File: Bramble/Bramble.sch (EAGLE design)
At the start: 10 parts

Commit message: Upgrades
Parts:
- added C1, C2, C3, C4, C5, C6, C7, C8: (no value), cap-master:CBP-ENP-020-050
- added F1: FUSEBLANK_5X20MM, fuse:FUSEBLANK_5X20MM
- added L1, L2, L3, L4, L5, L6, L7, L8: BL01RN1A, inductors:BL01RN1A
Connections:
- new net N$1: C1.1, L1.1, PWR1.VBUS
- new net N$2: C2.1, L2.1, PWR2.VBUS
- new net N$3: C4.1, L4.1, PWR4.VBUS
- new net N$4: C3.1, L3.1, PWR3.VBUS
- new net N$5: C5.1, L5.1, PWR5.VBUS
- new net N$6: C6.1, L6.1, PWR6.VBUS
- new net N$7: C7.1, L7.1, PWR7.VBUS
- new net N$8: C8.1, L8.1, PWR8.VBUS
- new net N$9: F1.2, PWR_IN-1.KL
- net 5V: now also L1.2, L2.2, L3.2, L4.2, L5.2, L6.2, L7.2, L8.2; no longer PWR1.VBUS, PWR2.VBUS, PWR3.VBUS, PWR4.VBUS, PWR5.VBUS, PWR6.VBUS, PWR7.VBUS, PWR8.VBUS, PWR_IN-1.KL
- net GND: now also C1.2, C2.2, C3.2, C4.2, C5.2, C6.2, C7.2, C8.2
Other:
- moved on the sheet: PWR1, PWR2, PWR3, PWR4

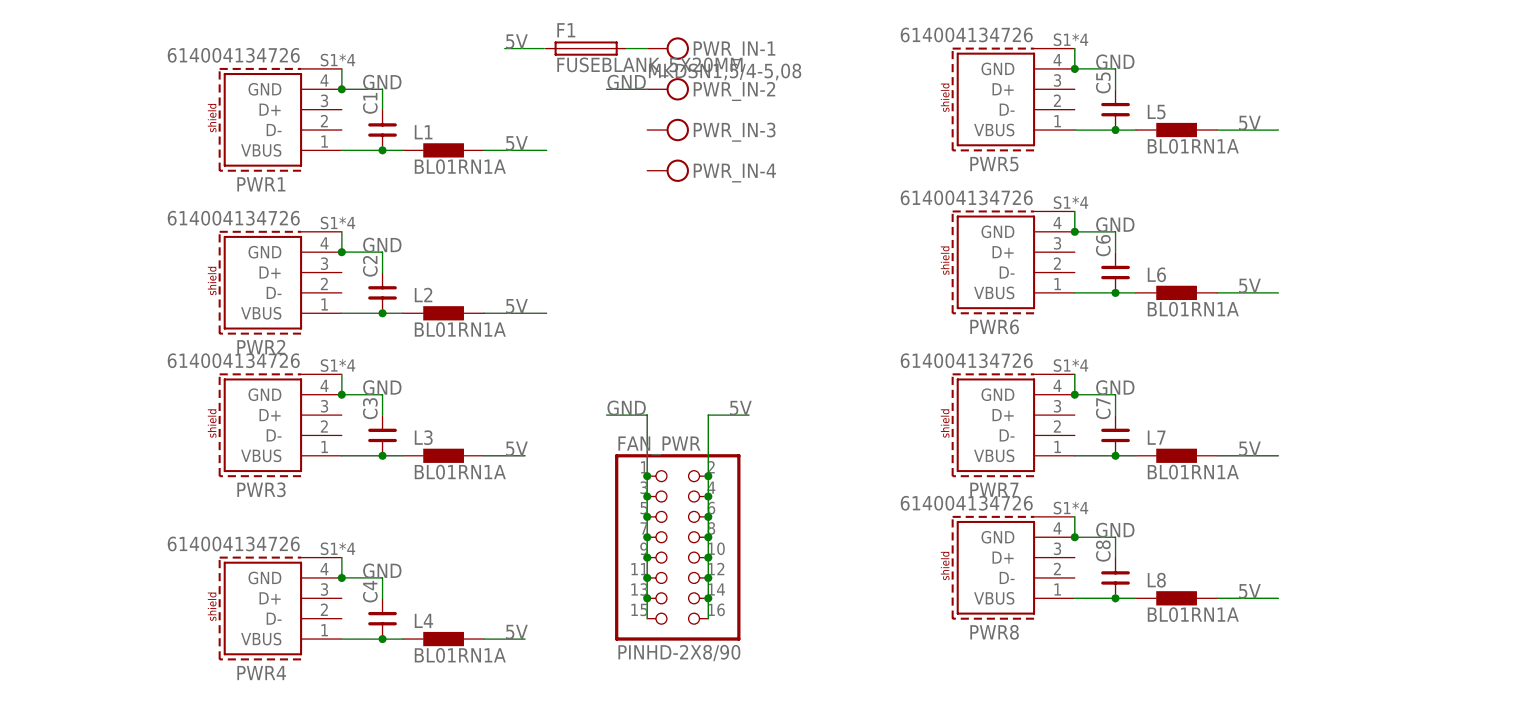
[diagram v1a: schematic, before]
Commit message: Capacitors among USB connectors
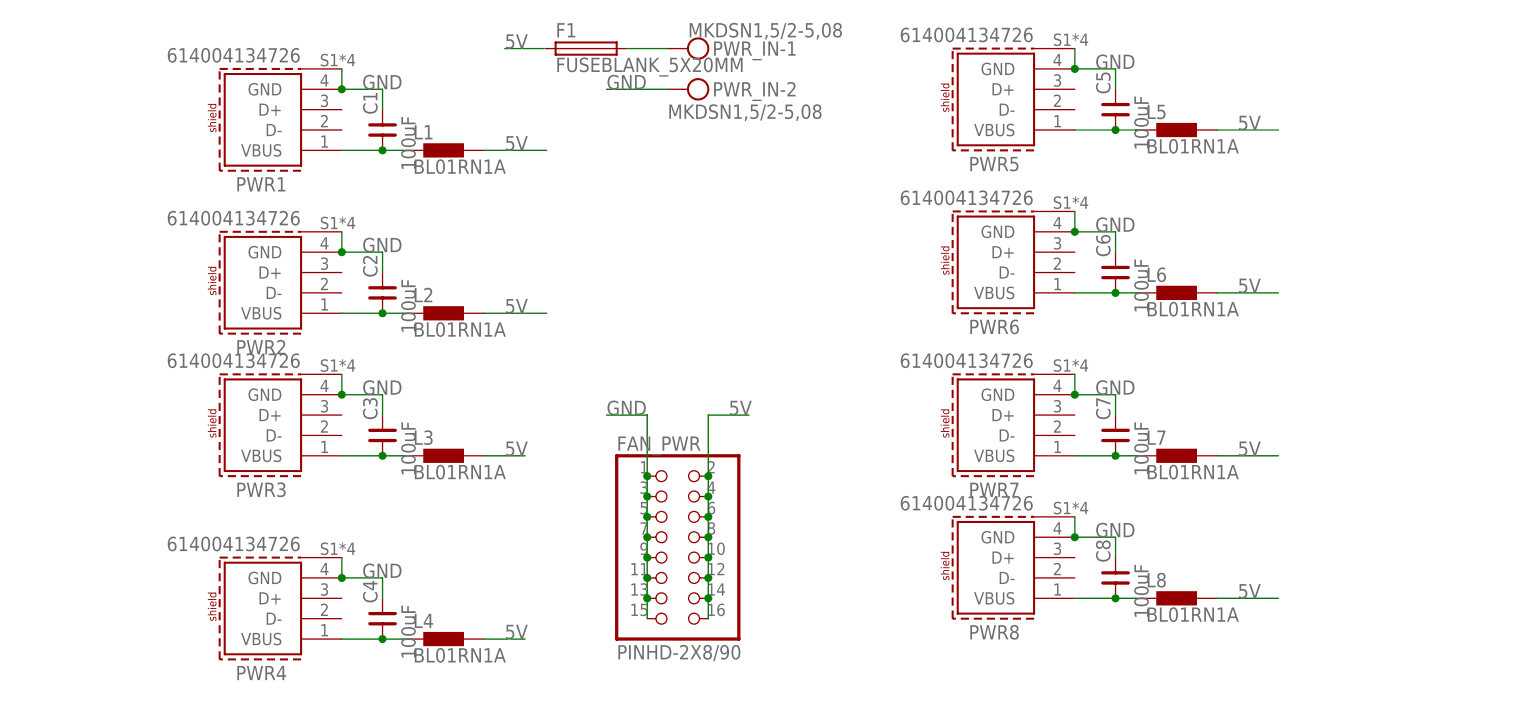
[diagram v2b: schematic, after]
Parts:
- C1, C2, C3, C4, C5, C6, C7, C8: value (none) -> 100uF
- PWR_IN: value MKDSN1,5/4-5,08 -> MKDSN1,5/2-5,08; device con-phoenix-508:MKDSN1,5/4-5,08 -> con-phoenix-508:MKDSN1,5/2-5,08
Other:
- moved on the sheet: PWR_IN-1, PWR_IN-2
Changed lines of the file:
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@@
 <grid distance="0.1" unitdist="inch" unit="inch" style="lines" multiple="1" display="no" altdistance="0.01" altunitdist="inch" altunit="inch"/>
 <layers>
-<layer number="1" name="Top" color="4" fill="1" visible="yes" active="no"/>
-<layer number="16" name="Bottom" color="1" fill="1" visible="yes" active="no"/>
-<layer number="17" name="Pads" color="2" fill="1" visible="yes" active="no"/>
-<layer number="18" name="Vias" color="2" fill="1" visible="yes" active="no"/>
-<layer number="19" name="Unrouted" color="6" fill="1" visible="yes" active="no"/>
-<layer number="20" name="Dimension" color="24" fill="1" visible="yes" active="no"/>
-<layer number="21" name="tPlace" color="7" fill="1" visible="yes" active="no"/>
-<layer number="22" name="bPlace" color="7" fill="1" visible="yes" active="no"/>
-<layer number="23" name="tOrigins" color="15" fill="1" visible="yes" active="no"/>
-<layer number="24" name="bOrigins" color="15" fill="1" visible="yes" active="no"/>
-<layer number="25" name="tNames" color="7" fill="1" visible="yes" active="no"/>
-<layer number="26" name="bNames" color="7" fill="1" visible="yes" active="no"/>
-<layer number="27" name="tValues" color="7" fill="1" visible="yes" active="no"/>
-<layer number="28" name="bValues" color="7" fill="1" visible="yes" active="no"/>
+<layer number="1" name="Top" color="4" fill="1" visible="no" active="no"/>
+<layer number="16" name="Bottom" color="1" fill="1" visible="no" active="no"/>
+<layer number="17" name="Pads" color="2" fill="1" visible="no" active="no"/>
+<layer number="18" name="Vias" color="2" fill="1" visible="no" active="no"/>
+<layer number="19" name="Unrouted" color="6" fill="1" visible="no" active="no"/>
+<layer number="20" name="Dimension" color="24" fill="1" visible="no" active="no"/>
+<layer number="21" name="tPlace" color="7" fill="1" visible="no" active="no"/>
+<layer number="22" name="bPlace" color="7" fill="1" visible="no" active="no"/>
+<layer number="23" name="tOrigins" color="15" fill="1" visible="no" active="no"/>
+<layer number="24" name="bOrigins" color="15" fill="1" visible="no" active="no"/>
+<layer number="25" name="tNames" color="7" fill="1" visible="no" active="no"/>
+<layer number="26" name="bNames" color="7" fill="1" visible="no" active="no"/>
+<layer number="27" name="tValues" color="7" fill="1" visible="no" active="no"/>
+<layer number="28" name="bValues" color="7" fill="1" visible="no" active="no"/>
 <layer number="29" name="tStop" color="7" fill="3" visible="no" active="no"/>
 <layer number="30" name="bStop" color="7" fill="6" visible="no" active="no"/>
@@
 <layer number="35" name="tGlue" color="7" fill="4" visible="no" active="no"/>
 <layer number="36" name="bGlue" color="7" fill="5" visible="no" active="no"/>
-<layer number="37" name="tTest" color="7" fill="1" visible="yes" active="no"/>
-<layer number="38" name="bTest" color="7" fill="1" visible="yes" active="no"/>
+<layer number="37" name="tTest" color="7" fill="1" visible="no" active="no"/>
+<layer number="38" name="bTest" color="7" fill="1" visible="no" active="no"/>
 <layer number="39" name="tKeepout" color="4" fill="11" visible="no" active="no"/>
 <layer number="40" name="bKeepout" color="1" fill="11" visible="no" active="no"/>
@@
 <layer number="44" name="Drills" color="7" fill="1" visible="no" active="no"/>
 <layer number="45" name="Holes" color="7" fill="1" visible="no" active="no"/>
-<layer number="46" name="Milling" color="3" fill="1" visible="yes" active="no"/>
-<layer number="47" name="Measures" color="7" fill="1" visible="yes" active="no"/>
-<layer number="48" name="Document" color="7" fill="1" visible="yes" active="no"/>
-<layer number="49" name="Reference" color="7" fill="1" visible="yes" active="no"/>
-<layer number="50" name="dxf" color="7" fill="1" visible="yes" active="no"/>
-<layer number="51" name="tDocu" color="7" fill="1" visible="yes" active="no"/>
-<layer number="52" name="bDocu" color="7" fill="1" visible="yes" active="no"/>
-<layer number="53" name="tGND_GNDA" color="7" fill="9" visible="yes" active="no"/>
-<layer number="54" name="bGND_GNDA" color="1" fill="9" visible="yes" active="no"/>
-<layer number="56" name="wert" color="7" fill="1" visible="yes" active="no"/>
+<layer number="46" name="Milling" color="3" fill="1" visible="no" active="no"/>
+<layer number="47" name="Measures" color="7" fill="1" visible="no" active="no"/>
+<layer number="48" name="Document" color="7" fill="1" visible="no" active="no"/>
+<layer number="49" name="Reference" color="7" fill="1" visible="no" active="no"/>
+<layer number="50" name="dxf" color="7" fill="1" visible="no" active="no"/>
+<layer number="51" name="tDocu" color="7" fill="1" visible="no" active="no"/>
+<layer number="52" name="bDocu" color="7" fill="1" visible="no" active="no"/>
+<layer number="53" name="tGND_GNDA" color="7" fill="9" visible="no" active="no"/>
+<layer number="54" name="bGND_GNDA" color="1" fill="9" visible="no" active="no"/>
+<layer number="56" name="wert" color="7" fill="1" visible="no" active="no"/>
 <layer number="88" name="SimResults" color="9" fill="1" visible="yes" active="yes"/>
 <layer number="89" name="SimProbes" color="9" fill="1" visible="yes" active="yes"/>
@@
 </classes>
 <parts>
-<part name="PWR_IN" library="con-phoenix-508" library_urn="urn:adsk.eagle:library:176" deviceset="MKDSN1,5/4-5,08" device="" package3d_urn="urn:adsk.eagle:package:9636/1"/>
 <part name="PWR1" library="Wurth_Connectors_WR-USB" library_urn="urn:adsk.eagle:library:16513831" deviceset="614004134726" device="" package3d_urn="urn:adsk.eagle:package:16513918/4" value="614004134726"/>
 <part name="PWR2" library="Wurth_Connectors_WR-USB" library_urn="urn:adsk.eagle:library:16513831" deviceset="614004134726" device="" package3d_urn="urn:adsk.eagle:package:16513918/4" value="614004134726"/>
@@
 <part name="L8" library="inductors" library_urn="urn:adsk.eagle:library:243" deviceset="BL0" device="1RN1A" package3d_urn="urn:adsk.eagle:package:15124/1"/>
 <part name="F1" library="fuse" library_urn="urn:adsk.eagle:library:233" deviceset="FUSE" device="BLANK_5X20MM" package3d_urn="urn:adsk.eagle:package:14079/1"/>
-<part name="C1" library="cap-master" deviceset="CBP-" device="ENP-020-050"/>
-<part name="C2" library="cap-master" deviceset="CBP-" device="ENP-020-050"/>
-<part name="C3" library="cap-master" deviceset="CBP-" device="ENP-020-050"/>
-<part name="C4" library="cap-master" deviceset="CBP-" device="ENP-020-050"/>
-<part name="C5" library="cap-master" deviceset="CBP-" device="ENP-020-050"/>
-<part name="C6" library="cap-master" deviceset="CBP-" device="ENP-020-050"/>
-<part name="C7" library="cap-master" deviceset="CBP-" device="ENP-020-050"/>
-<part name="C8" library="cap-master" deviceset="CBP-" device="ENP-020-050"/>
+<part name="C1" library="cap-master" deviceset="CBP-" device="ENP-020-050" value="100uF"/>
+<part name="C2" library="cap-master" deviceset="CBP-" device="ENP-020-050" value="100uF"/>
+<part name="C3" library="cap-master" deviceset="CBP-" device="ENP-020-050" value="100uF"/>
+<part name="C4" library="cap-master" deviceset="CBP-" device="ENP-020-050" value="100uF"/>
+<part name="C5" library="cap-master" deviceset="CBP-" device="ENP-020-050" value="100uF"/>
+<part name="C6" library="cap-master" deviceset="CBP-" device="ENP-020-050" value="100uF"/>
+<part name="C7" library="cap-master" deviceset="CBP-" device="ENP-020-050" value="100uF"/>
+<part name="C8" library="cap-master" deviceset="CBP-" device="ENP-020-050" value="100uF"/>
+<part name="PWR_IN" library="con-phoenix-508" library_urn="urn:adsk.eagle:library:176" deviceset="MKDSN1,5/2-5,08" device="" package3d_urn="urn:adsk.eagle:package:9630/1"/>
 </parts>
 <sheets>
@@
 </plain>
 <instances>
-<instance part="PWR_IN" gate="-1" x="43.18" y="76.2" smashed="yes">
-<attribute name="NAME" x="46.228" y="75.311" size="1.778" layer="95"/>
-<attribute name="VALUE" x="40.64" y="72.517" size="1.778" layer="96"/>
-</instance>
-<instance part="PWR_IN" gate="-2" x="43.18" y="71.12" smashed="yes">
-<attribute name="NAME" x="46.228" y="70.231" size="1.778" layer="95"/>
-</instance>
-<instance part="PWR_IN" gate="-3" x="43.18" y="66.04" smashed="yes">
-<attribute name="NAME" x="46.228" y="65.151" size="1.778" layer="95"/>
-</instance>
-<instance part="PWR_IN" gate="-4" x="43.18" y="60.96" smashed="yes">
-<attribute name="NAME" x="46.228" y="60.071" size="1.778" layer="95"/>
-</instance>
 <instance part="PWR1" gate="G$1" x="-7.62" y="66.04" smashed="yes" rot="R180">
 <attribute name="NAME" x="-7.5" y="60.15" size="1.778" layer="95" rot="R180" align="bottom-center"/>
@@
 <attribute name="NAME" x="98.425" y="12.065" size="1.778" layer="95" rot="R90"/>
 <attribute name="VALUE" x="103.1875" y="5.08" size="1.778" layer="96" rot="R90"/>
+</instance>
+<instance part="PWR_IN" gate="-1" x="45.72" y="76.2" smashed="yes">
+<attribute name="NAME" x="48.768" y="75.311" size="1.778" layer="95"/>
+<attribute name="VALUE" x="45.72" y="77.597" size="1.778" layer="96"/>
+</instance>
+<instance part="PWR_IN" gate="-2" x="45.72" y="71.12" smashed="yes">
+<attribute name="NAME" x="48.768" y="70.231" size="1.778" layer="95"/>
+<attribute name="VALUE" x="43.18" y="67.437" size="1.778" layer="96"/>
 </instance>
 </instances>
@@
 </segment>
 <segment>
-<wire x1="35.56" y1="71.12" x2="40.64" y2="71.12" width="0.1524" layer="91"/>
+<wire x1="35.56" y1="71.12" x2="43.18" y2="71.12" width="0.1524" layer="91"/>
+<label x="35.56" y="71.12" size="1.778" layer="95"/>
 <pinref part="PWR_IN" gate="-2" pin="KL"/>
-<label x="35.56" y="71.12" size="1.778" layer="95"/>
 </segment>
 <segment>
@@
 <net name="N$9" class="0">
 <segment>
+<pinref part="F1" gate="G$1" pin="2"/>
+<wire x1="38.1" y1="76.2" x2="43.18" y2="76.2" width="0.1524" layer="91"/>
 <pinref part="PWR_IN" gate="-1" pin="KL"/>
-<pinref part="F1" gate="G$1" pin="2"/>
-<wire x1="38.1" y1="76.2" x2="40.64" y2="76.2" width="0.1524" layer="91"/>
-</segment>
-</net>
+</segment>
+</net>

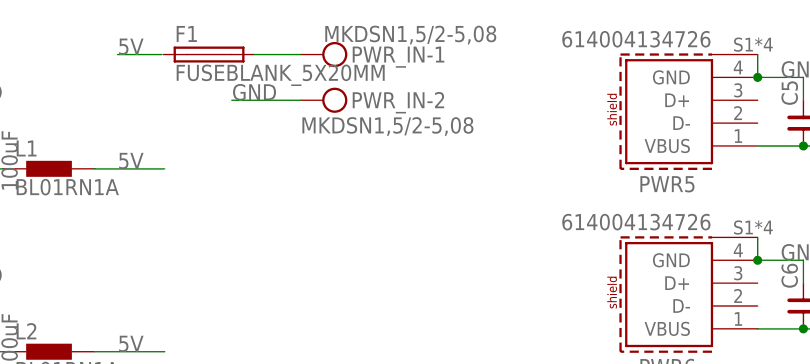
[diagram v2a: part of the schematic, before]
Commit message: Rotated PWR IN connector
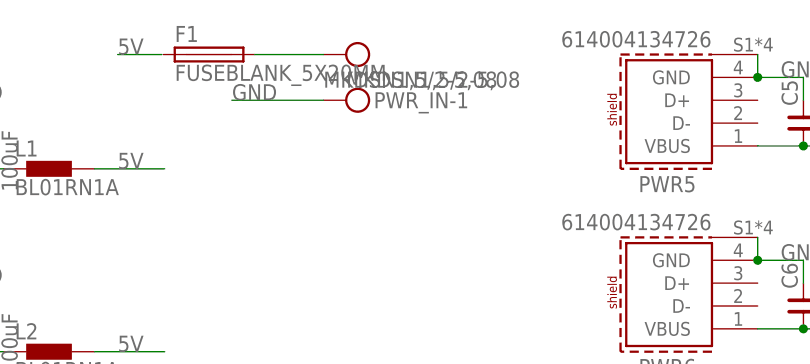
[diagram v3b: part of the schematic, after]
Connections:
- net GND: now also PWR_IN-1.KL; no longer PWR_IN-2.KL
- net N$9: now also PWR_IN-2.KL; no longer PWR_IN-1.KL
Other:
- moved on the sheet: PWR_IN-1
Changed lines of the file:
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@@
 <attribute name="VALUE" x="103.1875" y="5.08" size="1.778" layer="96" rot="R90"/>
 </instance>
-<instance part="PWR_IN" gate="-1" x="45.72" y="76.2" smashed="yes">
-<attribute name="NAME" x="48.768" y="75.311" size="1.778" layer="95"/>
-<attribute name="VALUE" x="45.72" y="77.597" size="1.778" layer="96"/>
+<instance part="PWR_IN" gate="-1" x="48.26" y="71.12" smashed="yes">
+<attribute name="NAME" x="51.308" y="70.231" size="1.778" layer="95"/>
+<attribute name="VALUE" x="48.26" y="72.517" size="1.778" layer="96"/>
 </instance>
-<instance part="PWR_IN" gate="-2" x="45.72" y="71.12" smashed="yes">
-<attribute name="NAME" x="48.768" y="70.231" size="1.778" layer="95"/>
-<attribute name="VALUE" x="43.18" y="67.437" size="1.778" layer="96"/>
+<instance part="PWR_IN" gate="-2" x="48.26" y="76.2" smashed="yes">
+<attribute name="VALUE" x="45.72" y="72.517" size="1.778" layer="96"/>
 </instance>
 </instances>
@@
 </segment>
 <segment>
-<wire x1="35.56" y1="71.12" x2="43.18" y2="71.12" width="0.1524" layer="91"/>
 <label x="35.56" y="71.12" size="1.778" layer="95"/>
-<pinref part="PWR_IN" gate="-2" pin="KL"/>
+<wire x1="35.56" y1="71.12" x2="45.72" y2="71.12" width="0.1524" layer="91"/>
+<pinref part="PWR_IN" gate="-1" pin="KL"/>
 </segment>
 <segment>
@@
 <segment>
 <pinref part="F1" gate="G$1" pin="2"/>
-<wire x1="38.1" y1="76.2" x2="43.18" y2="76.2" width="0.1524" layer="91"/>
-<pinref part="PWR_IN" gate="-1" pin="KL"/>
-</segment>
-</net>
+<wire x1="38.1" y1="76.2" x2="45.72" y2="76.2" width="0.1524" layer="91"/>
+<pinref part="PWR_IN" gate="-2" pin="KL"/>
+</segment>
+</net>

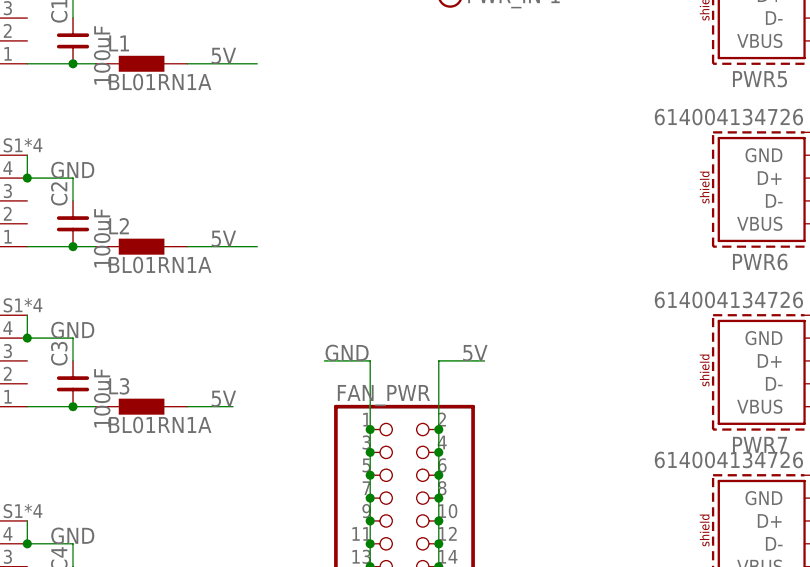
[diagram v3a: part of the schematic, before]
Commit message: Added capacitors for fans
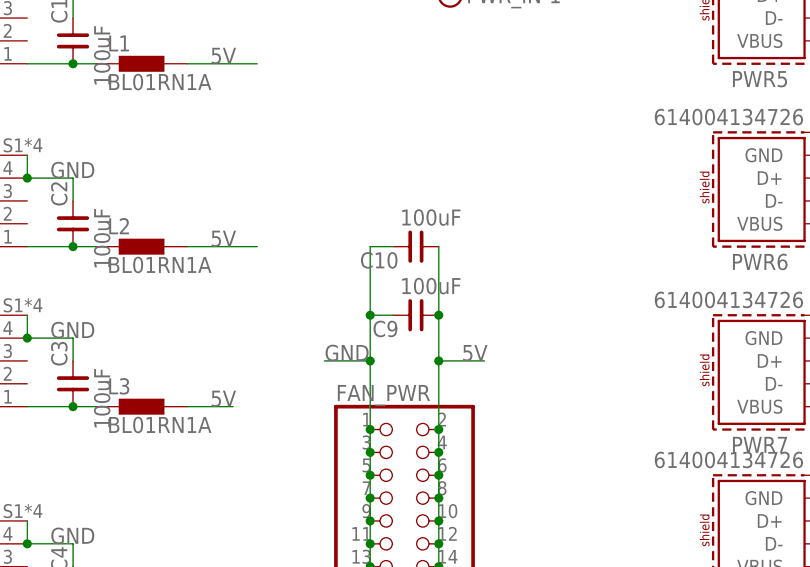
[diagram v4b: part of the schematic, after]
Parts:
- added C10, C9: 100uF, cap-master:CBP-ENP-020-050
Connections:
- net 5V: now also C10.1, C9.1
- net GND: now also C10.2, C9.2
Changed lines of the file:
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@@
 <part name="C8" library="cap-master" deviceset="CBP-" device="ENP-020-050" value="100uF"/>
 <part name="PWR_IN" library="con-phoenix-508" library_urn="urn:adsk.eagle:library:176" deviceset="MKDSN1,5/2-5,08" device="" package3d_urn="urn:adsk.eagle:package:9630/1"/>
+<part name="C9" library="cap-master" deviceset="CBP-" device="ENP-020-050" value="100uF"/>
+<part name="C10" library="cap-master" deviceset="CBP-" device="ENP-020-050" value="100uF"/>
 </parts>
 <sheets>
@@
 <instance part="PWR_IN" gate="-2" x="48.26" y="76.2" smashed="yes">
 <attribute name="VALUE" x="45.72" y="72.517" size="1.778" layer="96"/>
+</instance>
+<instance part="C9" gate="G$1" x="45.72" y="35.56" smashed="yes" rot="R180">
+<attribute name="NAME" x="43.815" y="34.925" size="1.778" layer="95" rot="R180"/>
+<attribute name="VALUE" x="50.8" y="39.6875" size="1.778" layer="96" rot="R180"/>
+</instance>
+<instance part="C10" gate="G$1" x="45.72" y="43.18" smashed="yes" rot="R180">
+<attribute name="NAME" x="43.815" y="42.545" size="1.778" layer="95" rot="R180"/>
+<attribute name="VALUE" x="50.8" y="47.3075" size="1.778" layer="96" rot="R180"/>
 </instance>
 </instances>
@@
 <junction x="48.26" y="7.62"/>
 <label x="50.8" y="30.48" size="1.778" layer="95"/>
+<pinref part="C10" gate="G$1" pin="1"/>
+<wire x1="48.26" y1="30.48" x2="48.26" y2="35.56" width="0.1524" layer="91"/>
+<junction x="48.26" y="30.48"/>
+<pinref part="C9" gate="G$1" pin="1"/>
+<wire x1="48.26" y1="35.56" x2="48.26" y2="43.18" width="0.1524" layer="91"/>
+<junction x="48.26" y="35.56"/>
 </segment>
 </net>
@@
 <junction x="40.64" y="7.62"/>
 <label x="35.56" y="30.48" size="1.778" layer="95"/>
+<pinref part="C10" gate="G$1" pin="2"/>
+<wire x1="43.18" y1="43.18" x2="40.64" y2="43.18" width="0.1524" layer="91"/>
+<wire x1="40.64" y1="43.18" x2="40.64" y2="35.56" width="0.1524" layer="91"/>
+<junction x="40.64" y="30.48"/>
+<pinref part="C9" gate="G$1" pin="2"/>
+<wire x1="40.64" y1="35.56" x2="40.64" y2="30.48" width="0.1524" layer="91"/>
+<wire x1="43.18" y1="35.56" x2="40.64" y2="35.56" width="0.1524" layer="91"/>
+<junction x="40.64" y="35.56"/>
 </segment>
 </net>
